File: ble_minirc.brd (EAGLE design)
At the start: 21 x 17.5 mm, 28 parts, among them CN1 B2B-PH-K-S, U1 DRV8835, U2 WT51822-S4, U3 MIC5205-3.3YM5-TR

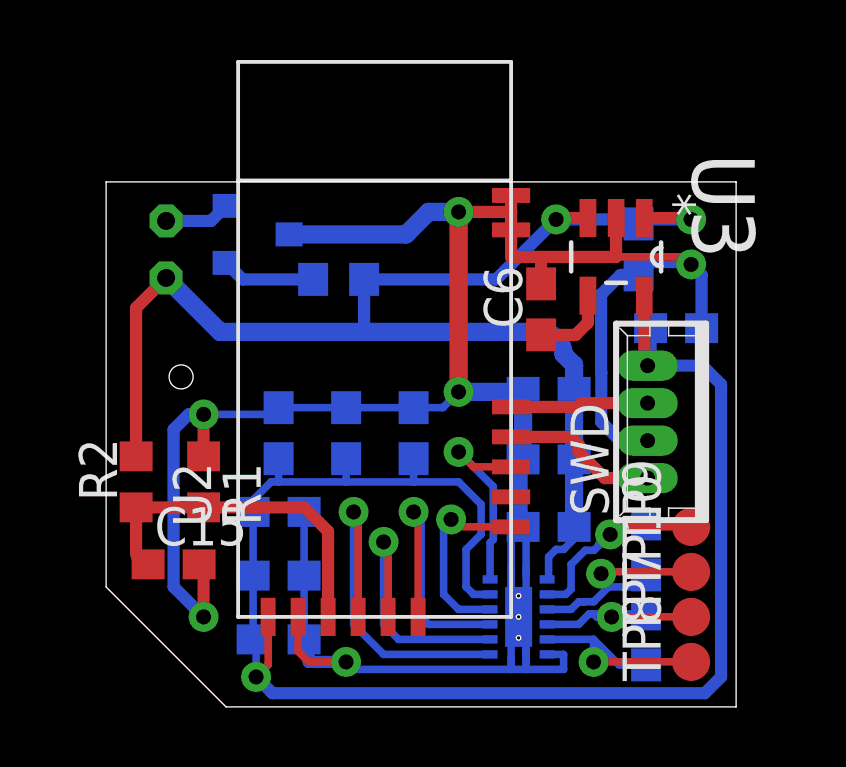
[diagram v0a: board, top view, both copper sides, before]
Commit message: Silkscreen cleanup
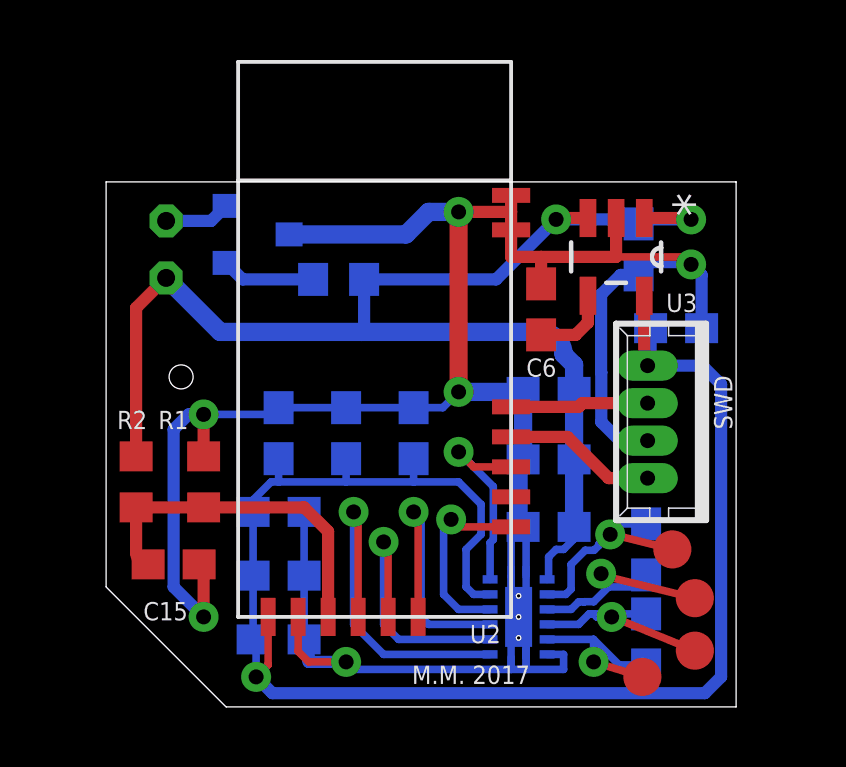
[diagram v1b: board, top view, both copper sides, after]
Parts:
- moved TP8 1.70 mm to (17.9, 1.00)
- moved TP7 1.13 mm to (19.6, 1.88)
- moved TP9 0.98 mm to (18.9, 5.25)
- moved TP10 0.88 mm to (19.6, 3.62)
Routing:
- net B2: track 7.65 -> 6.10 mm
- net A1: track 8.02 -> 7.02 mm
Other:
- board text added: "+"
- board text added: "M.M. 2017"

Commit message: Fixed FET direction
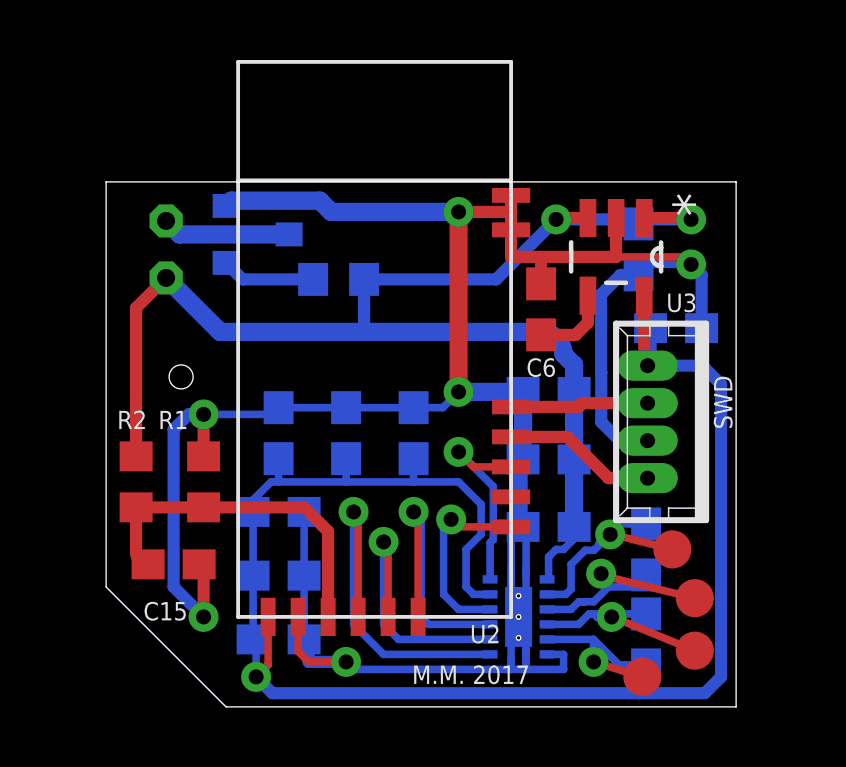
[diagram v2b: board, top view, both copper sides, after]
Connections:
- net AGND: now also Q3.3; no longer Q3.2
- net GND: now also Q3.2; no longer Q3.3
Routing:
- net AGND: track 2.21 -> 4.29 mm
- net GND: track 89.8 -> 91.8 mm
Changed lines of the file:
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@@
 <?xml version="1.0" encoding="utf-8"?>
 <!DOCTYPE eagle SYSTEM "eagle.dtd">
-<eagle version="8.4.1">
+<eagle version="8.7.0">
 <drawing>
 <settings>
@@
 <param name="checkRestrict" value="0"/>
 <param name="checkStop" value="0"/>
+<param name="checkValues" value="0"/>
 <param name="useDiameter" value="13"/>
 <param name="maxErrors" value="50"/>
@@
 </signal>
 <signal name="GND">
-<contactref element="Q3" pad="3"/>
 <contactref element="U2" pad="P2"/>
 <contactref element="U2" pad="P13"/>
@@
 <wire x1="6.6" y1="2.25" x2="6.6" y2="4.375" width="0.254" layer="16"/>
 <wire x1="6.6" y1="4.375" x2="6.6" y2="6.5" width="0.254" layer="16"/>
-<wire x1="6.1" y1="15.75" x2="10" y2="15.75" width="0.6096" layer="16"/>
-<wire x1="10" y1="15.75" x2="10.75" y2="16.5" width="0.6096" layer="16"/>
-<wire x1="10.75" y1="16.5" x2="11.75" y2="16.5" width="0.6096" layer="16"/>
 <via x="11.75" y="16.5" extent="1-16" drill="0.5" diameter="1" shape="octagon"/>
 <wire x1="11.75" y1="16.5" x2="13.5" y2="16.5" width="0.4064" layer="1"/>
@@
 <wire x1="15.25" y1="1.75" x2="15.25" y2="1.25" width="0.254" layer="16"/>
 <wire x1="15.25" y1="1.25" x2="14" y2="1.25" width="0.254" layer="16"/>
+<contactref element="Q3" pad="2"/>
+<wire x1="7.5" y1="16.5" x2="7.125" y2="16.875" width="0.6096" layer="16"/>
+<wire x1="7.125" y1="16.875" x2="4.175" y2="16.875" width="0.6096" layer="16"/>
+<wire x1="4.175" y1="16.875" x2="4" y2="16.7" width="0.6096" layer="16"/>
+<wire x1="11.75" y1="16.5" x2="7.5" y2="16.5" width="0.6096" layer="16"/>
 <wire x1="13.5" y1="17.0428" x2="13.5" y2="17.05" width="0" layer="19" extent="1-1"/>
 </signal>
 <signal name="AGND">
-<contactref element="Q3" pad="2"/>
 <contactref element="CN1" pad="1"/>
-<wire x1="2" y1="16.2" x2="3.5" y2="16.2" width="0.4064" layer="16"/>
-<wire x1="3.5" y1="16.2" x2="4" y2="16.7" width="0.4064" layer="16"/>
+<contactref element="Q3" pad="3"/>
+<wire x1="6.1" y1="15.75" x2="2.45" y2="15.75" width="0.6096" layer="16"/>
+<wire x1="2.45" y1="15.75" x2="2" y2="16.2" width="0.6096" layer="16"/>
 </signal>
 <signal name="SWDCLK">
